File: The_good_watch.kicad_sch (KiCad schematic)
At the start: 38 parts, among them IC1 DW01A, J1 Main, J2 USB_C_Receptacle_USB2.0, J3 PROG, J4 Screen, J5 Button, M1 Motor_DC, Q1 FS8205A, SW1 SW_Push, SW2 SW_Push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

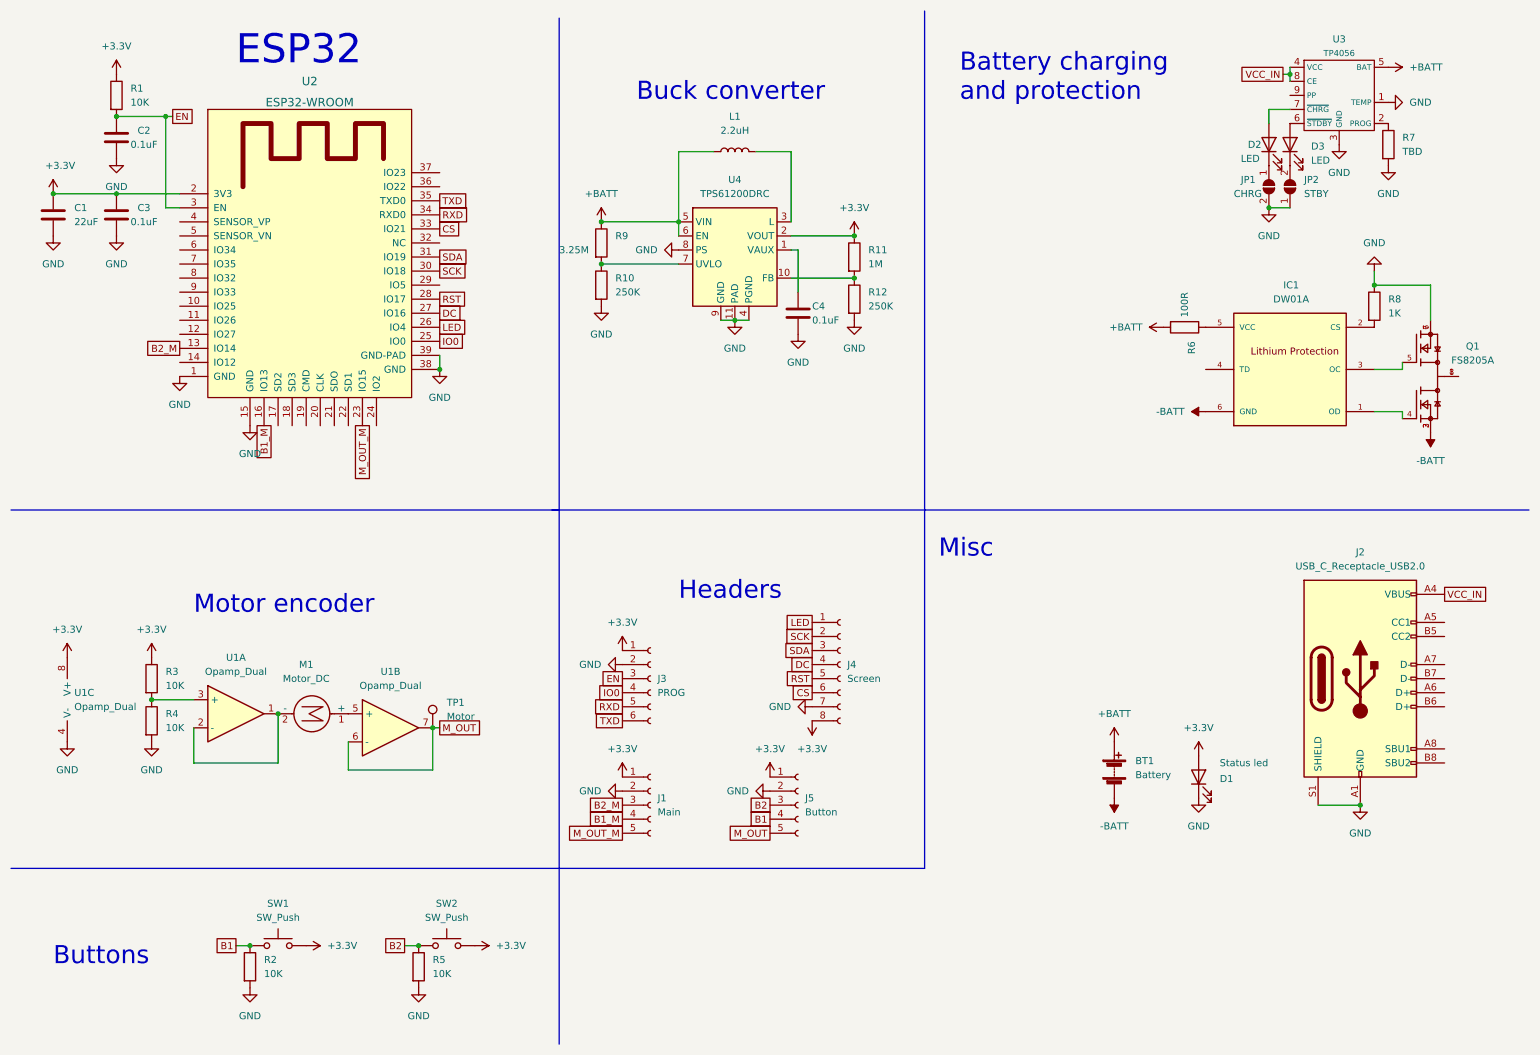
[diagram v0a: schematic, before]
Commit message: Added battery sense and regulator shutoff
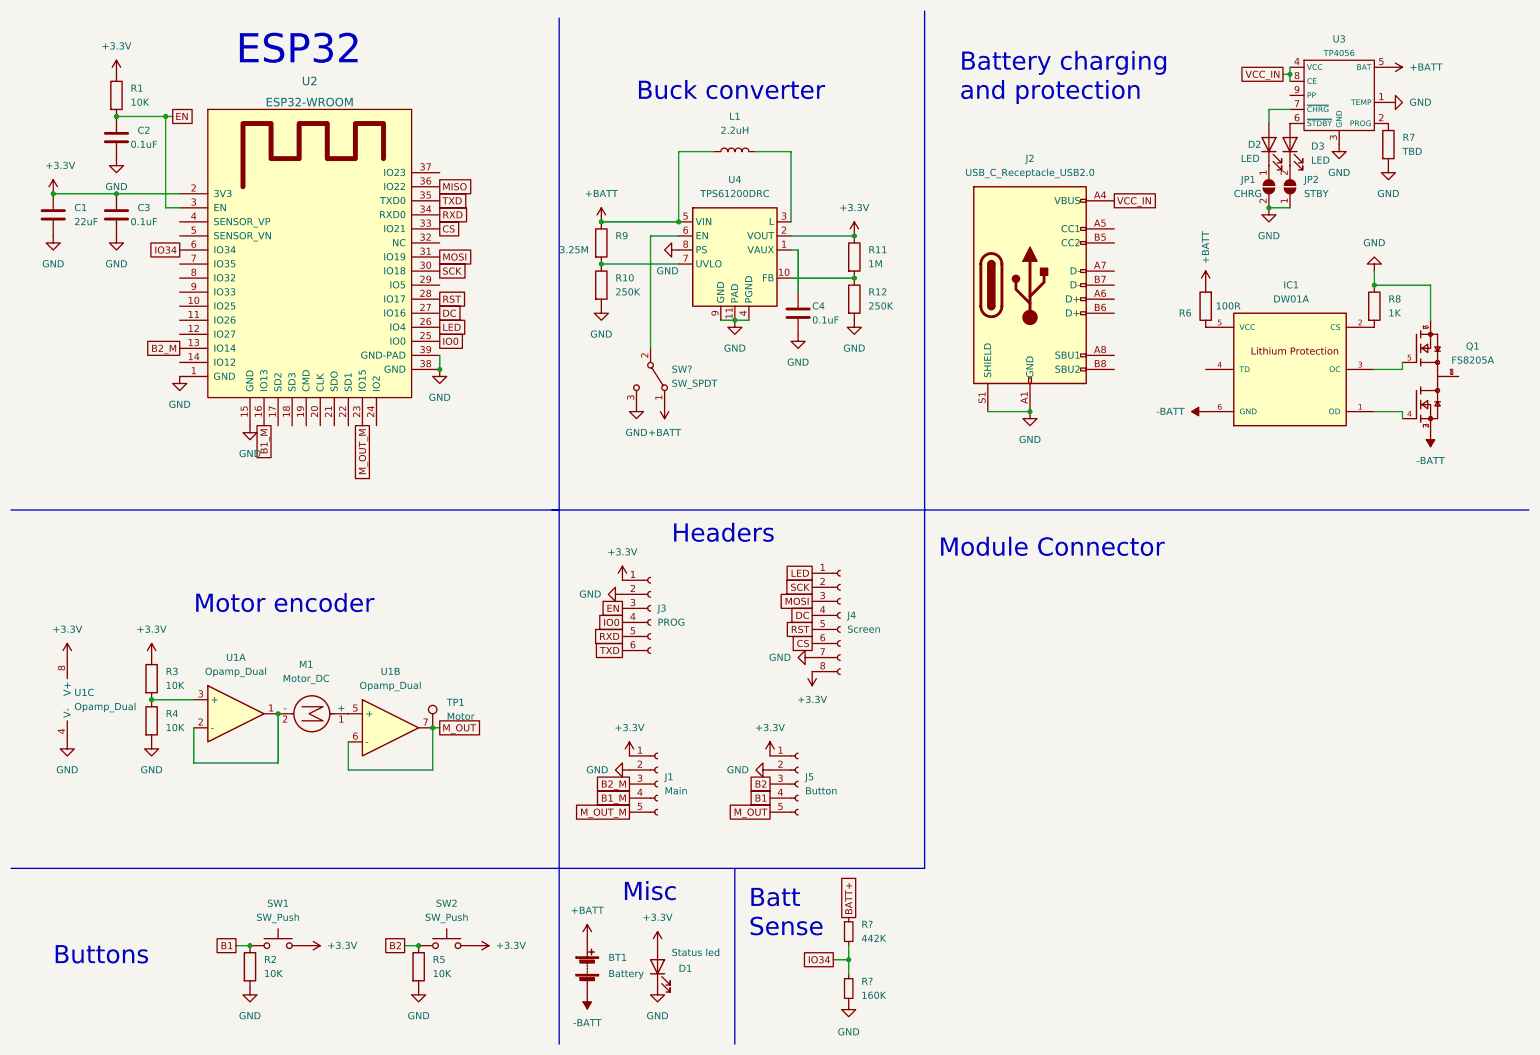
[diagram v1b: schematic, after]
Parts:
- added R?: 160K, Resistor_SMD:R_0402_1005Metric, symbol Device:R_Small
- added R?: 442K, Resistor_SMD:R_0402_1005Metric, symbol Device:R_Small
- added SW?: SW_SPDT, symbol Switch:SW_SPDT
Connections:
- net +BATT: now also SW?.1 (A); no longer U4.6 (EN)
- net GND: now also R?.2, SW?.3 (C)
- net MISO: now reaches U2.36 (IO22)
- net IO34: now reaches U2.6 (IO34)
- net IO34: now also R?.1, R?.2
- net SDA renamed MOSI
- new net: SW?.2 (B), U4.6 (EN)
- new net BATT+: R?.1
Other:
- note added: "Batt Sense"
- note added: "Module Connector"
- moved on the sheet: BT1, D1, J1, J2, J3, J4, J5, R6

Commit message: Connector layout trial
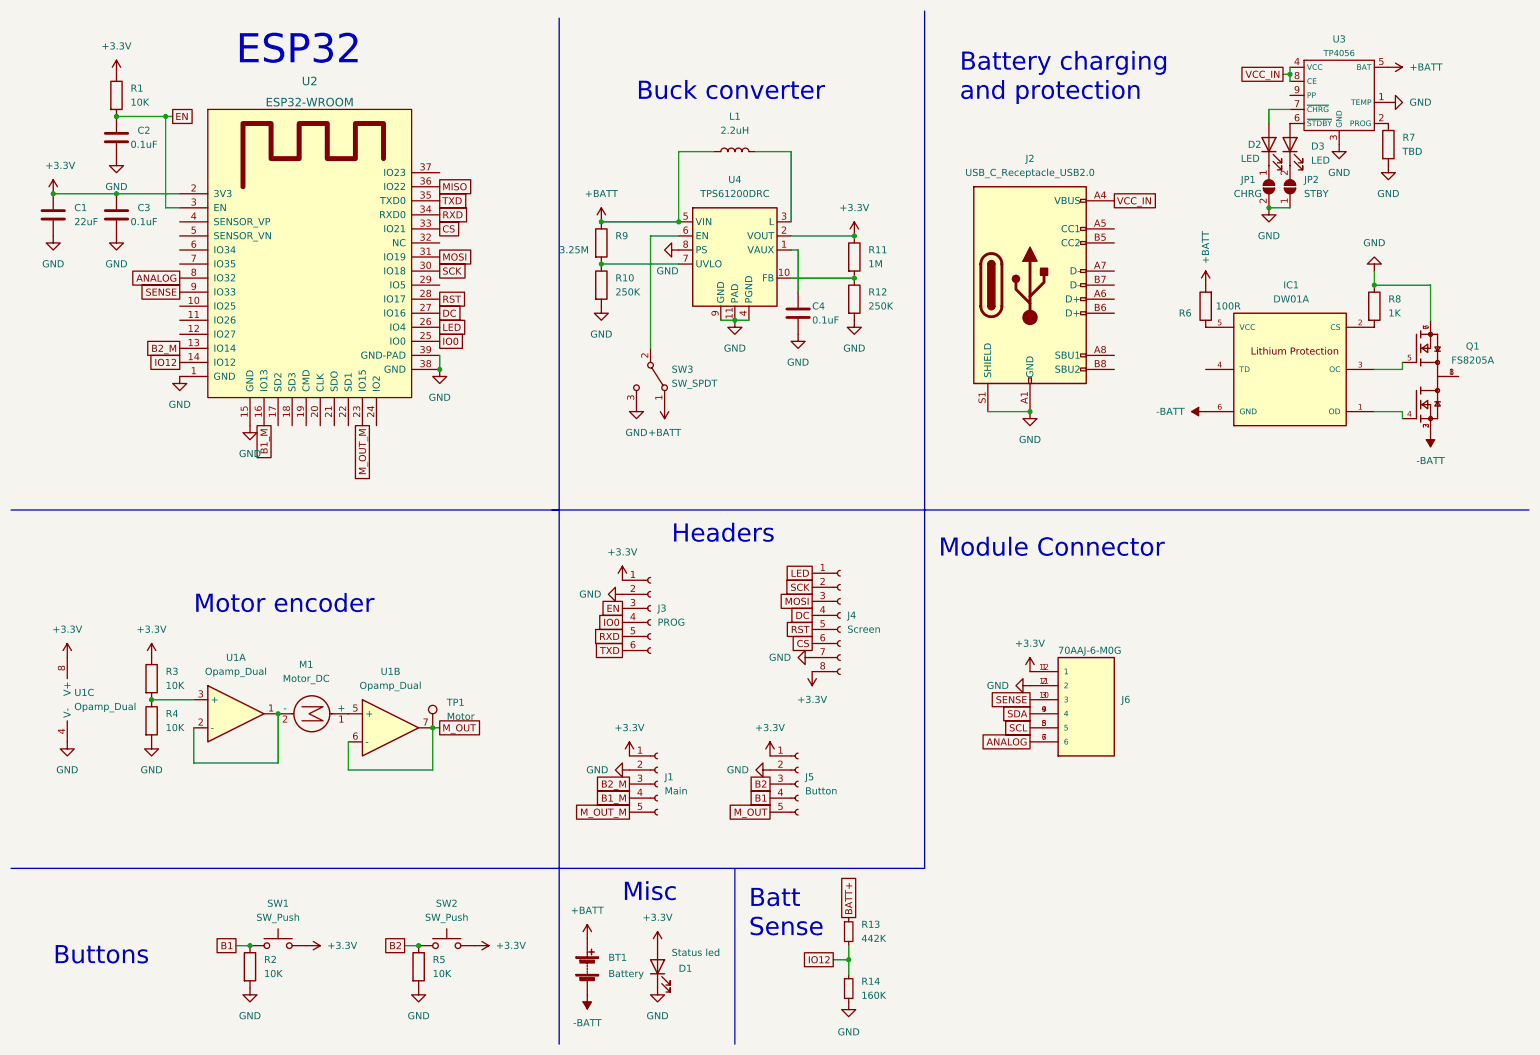
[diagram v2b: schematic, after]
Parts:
- added J6: 70AAJ-6-M0G, BOURNS_70AAJ-6-M0G, symbol 70AAJ-6-M0G:70AAJ-6-M0G
- gave numbers to parts that had none: 3
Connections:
- net +3V3: now also J6.1, J6.12 (1)
- net GND: now also J6.11 (2), J6.2
- net IO12: now reaches U2.14 (IO12)
- net IO12: now also R13.2, R14.1
- net ANALOG: now reaches U2.8 (IO32)
- net ANALOG: now also J6.6, J6.7 (6)
- net SENSE: now reaches U2.9 (IO33)
- net SENSE: now also J6.10 (3), J6.3
- removed net IO34: R13.2, R14.1, U2.6 (IO34)
- new net SCL: J6.5, J6.8 (5)
- new net SDA: J6.4, J6.9 (4)

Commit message: Finished layout and routing
Only minor graphical cleanup remains
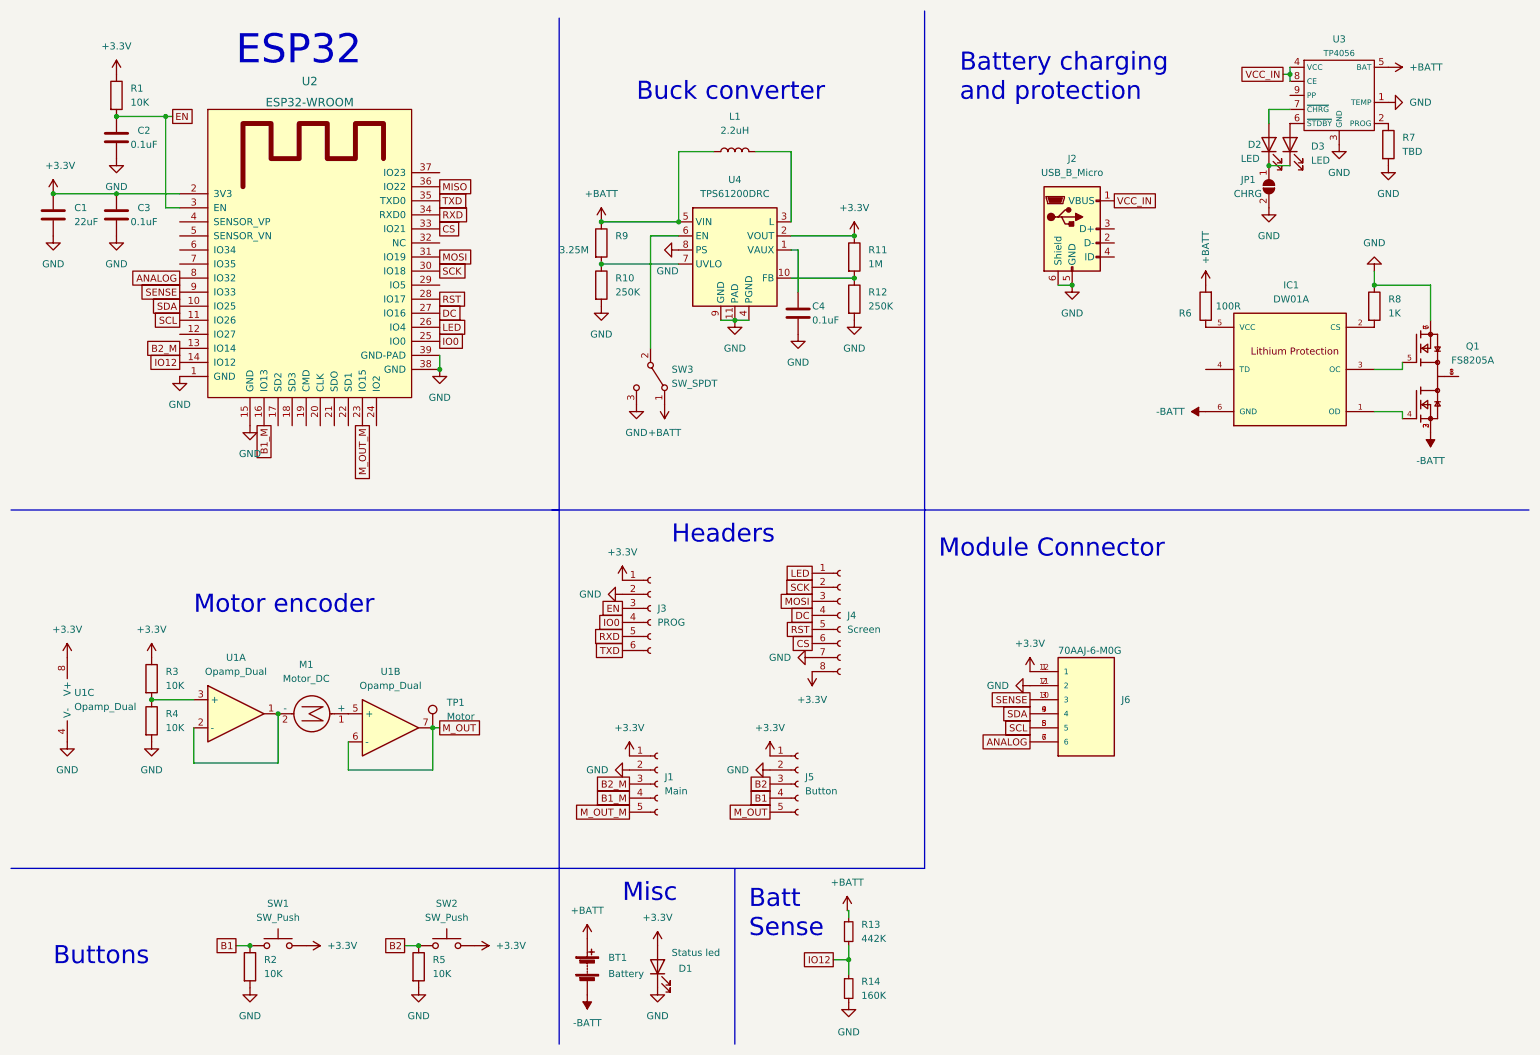
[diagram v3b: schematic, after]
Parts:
- removed J2: USB_C_Receptacle_USB2.0, Connector_USB:USB_C_Receptacle_GCT_USB4085, symbol Connector:USB_C_Receptacle_USB2.0
- removed JP2: STBY, Capacitor_SMD:C_1206_3216Metric, symbol Jumper:SolderJumper_2_Open
- added J2: USB_B_Micro, Connector_USB:USB_Micro-B_Amphenol_10104110_Horizontal, symbol Connector:USB_B_Micro
- J6: footprint BOURNS_70AAJ-6-M0G -> 70AAJ-6-M0G:BOURNS_70AAJ-6-M0G
- R6, R7, R8: footprint Resistor_SMD:R_1206_3216Metric_Pad1.30x1.75mm_HandSolder -> Resistor_SMD:R_0805_2012Metric
- SW3: footprint (none) -> Connector_PinHeader_2.00mm:PinHeader_1x03_P2.00mm_Vertical
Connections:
- net BATT+ is gone; now on net +BATT: R13.1
- net GND: now also J2.5 (GND), J2.6 (Shield)
- net SCL: now also U2.11 (IO26)
- net SDA: now also U2.10 (IO25)
- net VCC_IN: now also J2.1 (VBUS)
- net at D3.1 (K): now also D2.1 (K), JP1.1 (A)

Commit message: Changed spring connector for modules to pinheaders.
still need to update modules
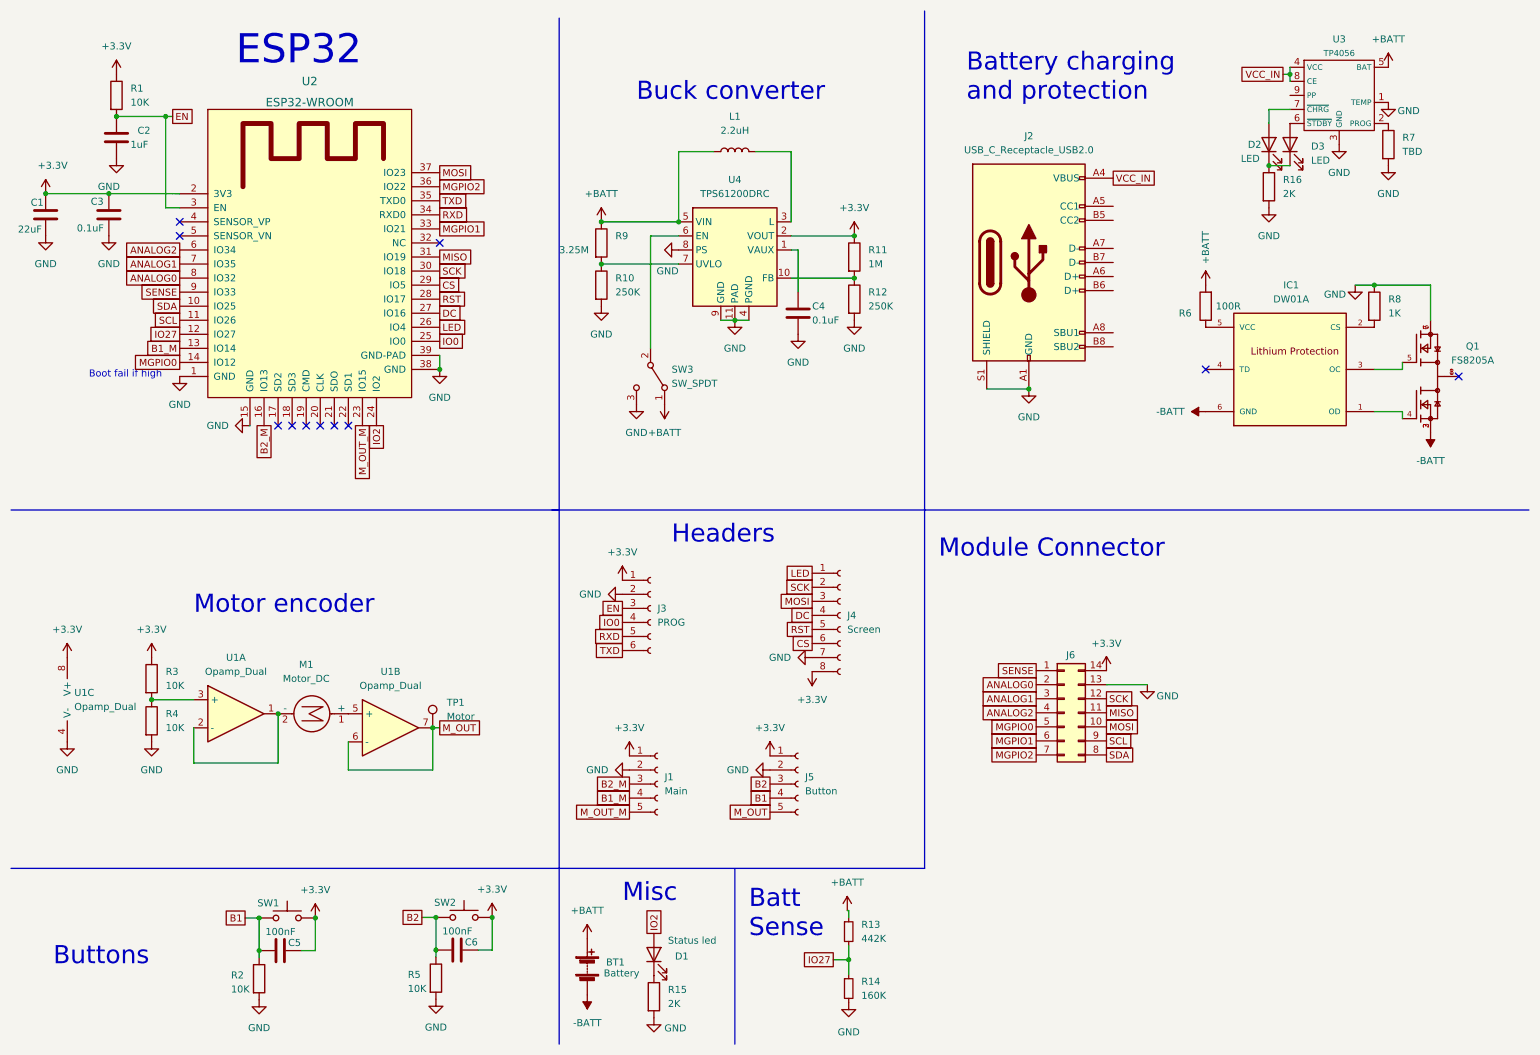
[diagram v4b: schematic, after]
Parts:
- removed J2: USB_B_Micro, Connector_USB:USB_Micro-B_Amphenol_10104110_Horizontal, symbol Connector:USB_B_Micro
- removed J6: 70AAJ-6-M0G, 70AAJ-6-M0G:BOURNS_70AAJ-6-M0G, symbol 70AAJ-6-M0G:70AAJ-6-M0G
- removed JP1: CHRG, Capacitor_SMD:C_1206_3216Metric, symbol Jumper:SolderJumper_2_Open
- added C5, C6: 100nF, Capacitor_SMD:C_0805_2012Metric_Pad1.18x1.45mm_HandSolder, symbol Device:C
- added J2: USB_C_Receptacle_USB2.0, Connector_USB:USB_C_Receptacle_GCT_USB4085, symbol Connector:USB_C_Receptacle_USB2.0
- added J6: Conn_02x07_Counter_Clockwise, Connector_PinHeader_1.27mm:PinHeader_2x07_P1.27mm_Horizontal, symbol Connector_Generic:Conn_02x07_Counter_Clockwise
- added R15, R16: 2K, Resistor_SMD:R_0805_2012Metric_Pad1.20x1.40mm_HandSolder, symbol Device:R
- C2: value 0.1uF -> 1uF
- R13, R14: footprint Resistor_SMD:R_0402_1005Metric -> Resistor_SMD:R_0402_1005Metric_Pad0.72x0.64mm_HandSolder
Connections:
- net +3V3: now also C5.2, C6.2, J6.14 (Pin_14); no longer D1.2 (A)
- net B1: now also C5.1
- net B1_M: now also U2.13 (IO14); no longer U2.16 (IO13)
- net B2: now also C6.1
- net B2_M: now also U2.16 (IO13); no longer U2.13 (IO14)
- net CS: now also U2.29 (IO5); no longer U2.33 (IO21)
- net GND: now also J2.A1 (GND), J2.A12 (GND), J2.B1 (GND), J2.B12 (GND), J2.S1 (SHIELD), J6.13 (Pin_13), R15.2, R16.2; no longer D1.1 (K)
- net MISO: now also U2.31 (IO19), J6.11 (Pin_11); no longer U2.36 (IO22)
- net MOSI: now also U2.37 (IO23), J6.10 (Pin_10); no longer U2.31 (IO19)
- net SCK: now also J6.12 (Pin_12)
- net SCL: now also J6.9 (Pin_9)
- net SDA: now also J6.8 (Pin_8)
- net SENSE: now also J6.1 (Pin_1)
- net VCC_IN: now also J2.A4 (VBUS), J2.A9 (VBUS), J2.B4 (VBUS), J2.B9 (VBUS)
- net IO27: now reaches U2.12 (IO27)
- net IO27: now also R13.2, R14.1
- net IO2: now reaches U2.24 (IO2)
- net IO2: now also D1.2 (A)
- net ANALOG2: now reaches U2.6 (IO34)
- net ANALOG2: now also J6.4 (Pin_4)
- net ANALOG1: now reaches U2.7 (IO35)
- net ANALOG1: now also J6.3 (Pin_3)
- net at D2.1 (K), D3.1 (K): now also R16.1
- net ANALOG renamed ANALOG0
- net ANALOG0: now also J6.2 (Pin_2)
- removed net IO12: R13.2, R14.1, U2.14 (IO12)
- new net: D1.1 (K), R15.1
- new net MGPIO0: J6.5 (Pin_5), U2.14 (IO12)
- new net MGPIO1: J6.6 (Pin_6), U2.33 (IO21)
- new net MGPIO2: J6.7 (Pin_7), U2.36 (IO22)
- no-connect marks 0 -> 11
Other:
- note added: "Boot fail if high"
- moved on the sheet: C1, C3, D1, R2, SW1

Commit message: Graphical fixes, minor electrical fixes and enviro sensor module trial
Fixed some component values and added i2c pullups
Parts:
- added R17, R18: 4.7K, Resistor_SMD:R_0805_2012Metric, symbol Device:R
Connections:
- net +3V3: now also R17.1, R18.1
- net SCL: now also R17.2
- net SDA: now also R18.2
- no-connect marks 11 -> 19
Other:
- note added: "Its misleading to call these analog but they are input only"
- note added: "R7 sets charge charge current see datasheet to find lookup table"
- moved on the sheet: J2, J6
